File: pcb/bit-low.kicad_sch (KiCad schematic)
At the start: 6 parts, among them Q893 2N7002b, Q894 2N7002b, Q895 2N7002b

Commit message: Faster.
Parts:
- Q886: renamed from Q893; value 2N7002b -> 2N7002K; LCSC C8545 -> C181083
- Q887: renamed from Q894; value 2N7002b -> 2N7002K; LCSC C8545 -> C181083
- Q888: renamed from Q895; value 2N7002b -> 2N7002K; LCSC C8545 -> C181083
- renumbered R399 to R396, R400 to R397
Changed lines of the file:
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@@
   (symbol (lib_id "power:VCC") (at 184.15 44.45 0)
     (in_bom yes) (on_board yes)
-    (property "Reference" "#PWR0826" (id 0) (at 184.15 48.26 0)
+    (property "Reference" "#PWR0818" (id 0) (at 184.15 48.26 0)
       (effects (font (size 1.27 1.27)) hide)
     )
@@
   (symbol (lib_id "power:VCC") (at 200.66 40.64 0)
     (in_bom yes) (on_board yes)
-    (property "Reference" "#PWR0825" (id 0) (at 200.66 44.45 0)
+    (property "Reference" "#PWR0817" (id 0) (at 200.66 44.45 0)
       (effects (font (size 1.27 1.27)) hide)
     )
@@
   (symbol (lib_id "power:VCC") (at 220.98 71.12 0)
     (in_bom yes) (on_board yes)
-    (property "Reference" "#PWR0828" (id 0) (at 220.98 74.93 0)
+    (property "Reference" "#PWR0820" (id 0) (at 220.98 74.93 0)
       (effects (font (size 1.27 1.27)) hide)
     )
@@
   (symbol (lib_id "power:GND") (at 95.25 140.97 0)
     (in_bom yes) (on_board yes)
-    (property "Reference" "#PWR0830" (id 0) (at 95.25 147.32 0)
+    (property "Reference" "#PWR0822" (id 0) (at 95.25 147.32 0)
       (effects (font (size 1.27 1.27)) hide)
     )
@@
   (symbol (lib_id "power:GND") (at 184.15 52.07 0)
     (in_bom yes) (on_board yes)
-    (property "Reference" "#PWR0827" (id 0) (at 184.15 58.42 0)
+    (property "Reference" "#PWR0819" (id 0) (at 184.15 58.42 0)
       (effects (font (size 1.27 1.27)) hide)
     )
@@
   (symbol (lib_id "power:GND") (at 220.98 109.22 0)
     (in_bom yes) (on_board yes)
-    (property "Reference" "#PWR0829" (id 0) (at 220.98 115.57 0)
+    (property "Reference" "#PWR0821" (id 0) (at 220.98 115.57 0)
       (effects (font (size 1.27 1.27)) hide)
     )
@@
   (symbol (lib_id "Device:R") (at 200.66 44.45 0)
     (in_bom yes) (on_board yes)
-    (property "Reference" "R399" (id 0) (at 202.438 43.2816 0)
+    (property "Reference" "R396" (id 0) (at 202.438 43.2816 0)
       (effects (font (size 1.27 1.27)) (justify left))
     )
@@
   (symbol (lib_id "Device:R") (at 220.98 74.93 0)
     (in_bom yes) (on_board yes)
-    (property "Reference" "R400" (id 0) (at 222.758 73.7616 0)
+    (property "Reference" "R397" (id 0) (at 222.758 73.7616 0)
       (effects (font (size 1.27 1.27)) (justify left))
     )
@@
   (symbol (lib_id "Transistor_FET:2N7002") (at 92.71 135.89 0)
     (in_bom yes) (on_board yes)
-    (property "Reference" "Q895" (id 0) (at 97.9424 134.7216 0)
-      (effects (font (size 1.27 1.27)) (justify left))
-    )
-    (property "Value" "2N7002b" (id 1) (at 97.942 137.033 0)
+    (property "Reference" "Q888" (id 0) (at 97.9424 134.7216 0)
+      (effects (font (size 1.27 1.27)) (justify left))
+    )
+    (property "Value" "2N7002K" (id 1) (at 97.942 137.033 0)
       (effects (font (size 1.27 1.27)) (justify left))
     )
@@
       (effects (font (size 1.27 1.27) italic) (justify left) hide)
     )
-    (property "Datasheet" "https://www.fairchildsemi.com/datasheets/2N/2N7002.pdf" (id 3) (at 92.71 135.89 0)
+    (property "Datasheet" "https://datasheet.lcsc.com/szlcsc/Guangdong-Hottech-2N7002K_C181083.pdf" (id 3) (at 92.71 135.89 0)
       (effects (font (size 1.27 1.27)) (justify left) hide)
     )
-    (property "LCSC" "C8545" (id 4) (at 92.71 135.89 0)
+    (property "LCSC" "C181083" (id 4) (at 92.71 135.89 0)
       (effects (font (size 1.27 1.27)) hide)
     )
@@
   (symbol (lib_id "Transistor_FET:2N7002") (at 218.44 93.98 0)
     (in_bom yes) (on_board yes)
-    (property "Reference" "Q893" (id 0) (at 223.6724 92.8116 0)
-      (effects (font (size 1.27 1.27)) (justify left))
-    )
-    (property "Value" "2N7002b" (id 1) (at 223.672 95.123 0)
+    (property "Reference" "Q886" (id 0) (at 223.6724 92.8116 0)
+      (effects (font (size 1.27 1.27)) (justify left))
+    )
+    (property "Value" "2N7002K" (id 1) (at 223.672 95.123 0)
       (effects (font (size 1.27 1.27)) (justify left))
     )
@@
       (effects (font (size 1.27 1.27) italic) (justify left) hide)
     )
-    (property "Datasheet" "https://www.fairchildsemi.com/datasheets/2N/2N7002.pdf" (id 3) (at 218.44 93.98 0)
+    (property "Datasheet" "https://datasheet.lcsc.com/szlcsc/Guangdong-Hottech-2N7002K_C181083.pdf" (id 3) (at 218.44 93.98 0)
       (effects (font (size 1.27 1.27)) (justify left) hide)
     )
-    (property "LCSC" "C8545" (id 4) (at 218.44 93.98 0)
+    (property "LCSC" "C181083" (id 4) (at 218.44 93.98 0)
       (effects (font (size 1.27 1.27)) hide)
     )
@@
   (symbol (lib_id "Transistor_FET:2N7002") (at 218.44 104.14 0)
     (in_bom yes) (on_board yes)
-    (property "Reference" "Q894" (id 0) (at 223.6724 102.9716 0)
-      (effects (font (size 1.27 1.27)) (justify left))
-    )
-    (property "Value" "2N7002b" (id 1) (at 223.672 105.283 0)
+    (property "Reference" "Q887" (id 0) (at 223.6724 102.9716 0)
+      (effects (font (size 1.27 1.27)) (justify left))
+    )
+    (property "Value" "2N7002K" (id 1) (at 223.672 105.283 0)
       (effects (font (size 1.27 1.27)) (justify left))
     )
@@
       (effects (font (size 1.27 1.27) italic) (justify left) hide)
     )
-    (property "Datasheet" "https://www.fairchildsemi.com/datasheets/2N/2N7002.pdf" (id 3) (at 218.44 104.14 0)
+    (property "Datasheet" "https://datasheet.lcsc.com/szlcsc/Guangdong-Hottech-2N7002K_C181083.pdf" (id 3) (at 218.44 104.14 0)
       (effects (font (size 1.27 1.27)) (justify left) hide)
     )
-    (property "LCSC" "C8545" (id 4) (at 218.44 104.14 0)
-      (effects (font (size 1.27 1.27)) hide)
-    )
+    (property "LCSC" "C181083" (id 4) (at 218.44 104.14 0)
+      (effects (font (size 1.27 1.27)) hide)
+    )

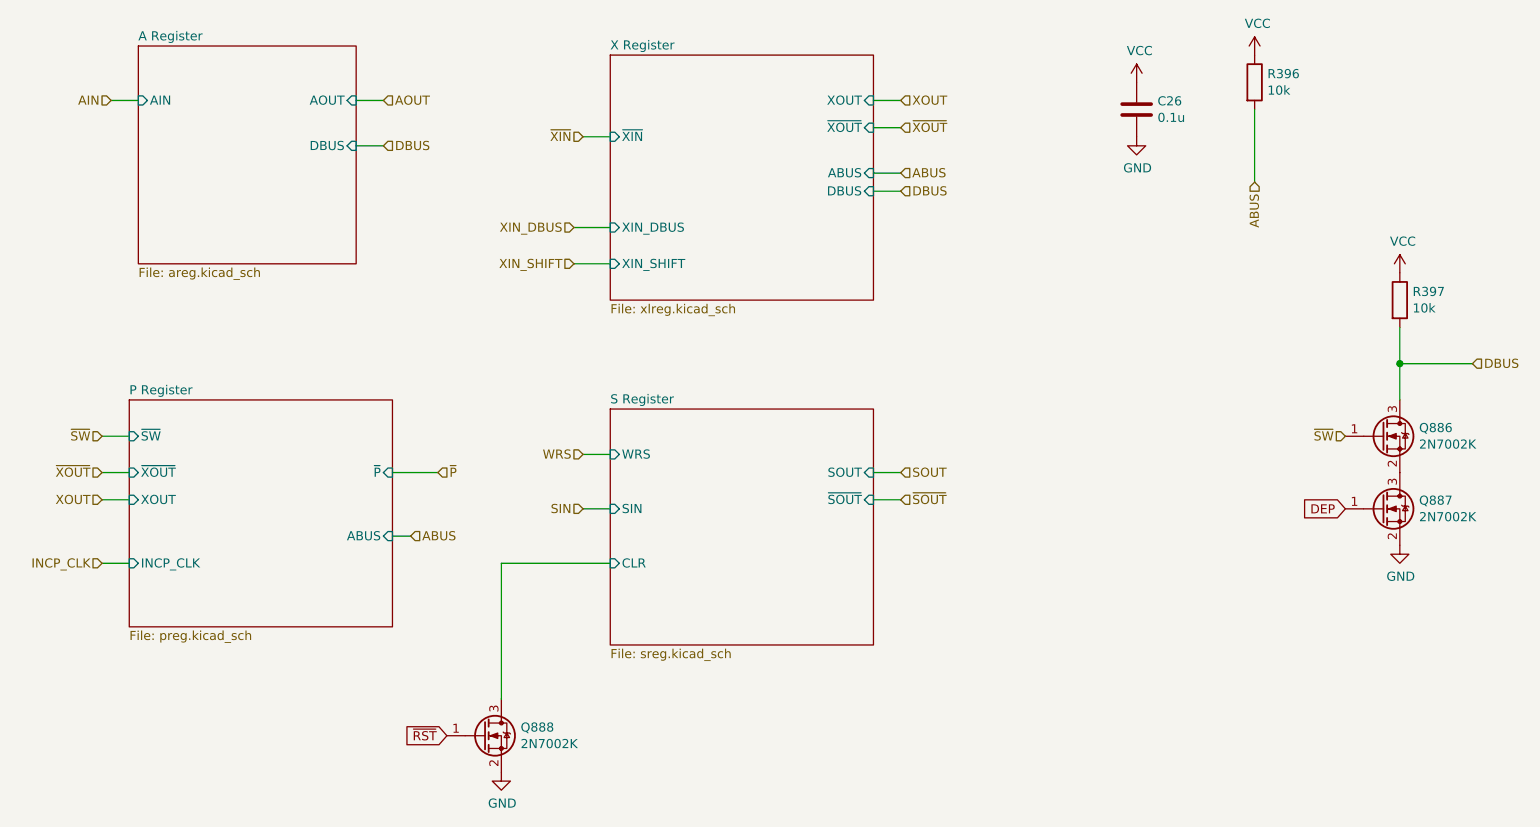
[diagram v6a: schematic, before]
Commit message: Fix flag for lea.
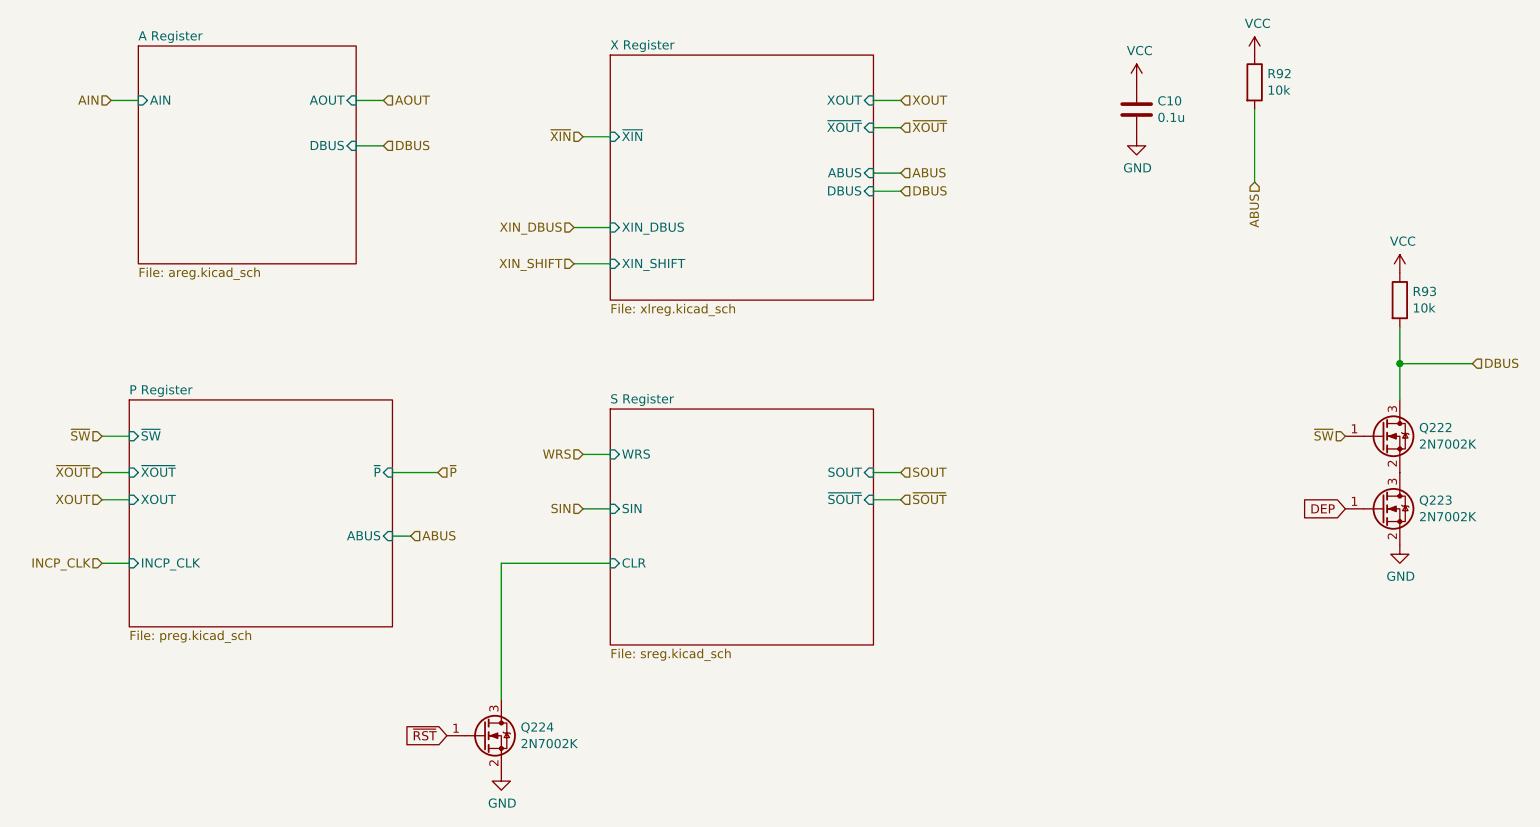
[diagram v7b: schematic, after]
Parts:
- renumbered C26 to C10, Q886 to Q222, Q887 to Q223, Q888 to Q224, R396 to R92, R397 to R93
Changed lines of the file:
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@@
   (symbol (lib_id "Device:R") (at 200.66 44.45 0)
     (in_bom yes) (on_board yes)
-    (property "Reference" "R396" (id 0) (at 202.438 43.2816 0)
+    (property "Reference" "R92" (id 0) (at 202.438 43.2816 0)
       (effects (font (size 1.27 1.27)) (justify left))
     )
@@
   (symbol (lib_id "Device:R") (at 220.98 74.93 0)
     (in_bom yes) (on_board yes)
-    (property "Reference" "R397" (id 0) (at 222.758 73.7616 0)
+    (property "Reference" "R93" (id 0) (at 222.758 73.7616 0)
       (effects (font (size 1.27 1.27)) (justify left))
     )
@@
   (symbol (lib_id "Device:C") (at 184.15 48.26 0)
     (in_bom yes) (on_board yes)
-    (property "Reference" "C26" (id 0) (at 187.071 47.0916 0)
+    (property "Reference" "C10" (id 0) (at 187.071 47.0916 0)
       (effects (font (size 1.27 1.27)) (justify left))
     )
@@
   (symbol (lib_id "Transistor_FET:2N7002") (at 92.71 135.89 0)
     (in_bom yes) (on_board yes)
-    (property "Reference" "Q888" (id 0) (at 97.9424 134.7216 0)
+    (property "Reference" "Q224" (id 0) (at 97.9424 134.7216 0)
       (effects (font (size 1.27 1.27)) (justify left))
     )
@@
   (symbol (lib_id "Transistor_FET:2N7002") (at 218.44 93.98 0)
     (in_bom yes) (on_board yes)
-    (property "Reference" "Q886" (id 0) (at 223.6724 92.8116 0)
+    (property "Reference" "Q222" (id 0) (at 223.6724 92.8116 0)
       (effects (font (size 1.27 1.27)) (justify left))
     )
@@
   (symbol (lib_id "Transistor_FET:2N7002") (at 218.44 104.14 0)
     (in_bom yes) (on_board yes)
-    (property "Reference" "Q887" (id 0) (at 223.6724 102.9716 0)
+    (property "Reference" "Q223" (id 0) (at 223.6724 102.9716 0)
       (effects (font (size 1.27 1.27)) (justify left))
     )

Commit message: Revision 3.
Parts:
- renumbered C10 to C26, Q222 to Q886, Q223 to Q887, Q224 to Q888, R92 to R396, R93 to R397
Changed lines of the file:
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@@
   (symbol (lib_id "Device:R") (at 200.66 44.45 0)
     (in_bom yes) (on_board yes)
-    (property "Reference" "R92" (id 0) (at 202.438 43.2816 0)
+    (property "Reference" "R396" (id 0) (at 202.438 43.2816 0)
       (effects (font (size 1.27 1.27)) (justify left))
     )
@@
   (symbol (lib_id "Device:R") (at 220.98 74.93 0)
     (in_bom yes) (on_board yes)
-    (property "Reference" "R93" (id 0) (at 222.758 73.7616 0)
+    (property "Reference" "R397" (id 0) (at 222.758 73.7616 0)
       (effects (font (size 1.27 1.27)) (justify left))
     )
@@
   (symbol (lib_id "Device:C") (at 184.15 48.26 0)
     (in_bom yes) (on_board yes)
-    (property "Reference" "C10" (id 0) (at 187.071 47.0916 0)
+    (property "Reference" "C26" (id 0) (at 187.071 47.0916 0)
       (effects (font (size 1.27 1.27)) (justify left))
     )
@@
   (symbol (lib_id "Transistor_FET:2N7002") (at 92.71 135.89 0)
     (in_bom yes) (on_board yes)
-    (property "Reference" "Q224" (id 0) (at 97.9424 134.7216 0)
+    (property "Reference" "Q888" (id 0) (at 97.9424 134.7216 0)
       (effects (font (size 1.27 1.27)) (justify left))
     )
@@
   (symbol (lib_id "Transistor_FET:2N7002") (at 218.44 93.98 0)
     (in_bom yes) (on_board yes)
-    (property "Reference" "Q222" (id 0) (at 223.6724 92.8116 0)
+    (property "Reference" "Q886" (id 0) (at 223.6724 92.8116 0)
       (effects (font (size 1.27 1.27)) (justify left))
     )
@@
   (symbol (lib_id "Transistor_FET:2N7002") (at 218.44 104.14 0)
     (in_bom yes) (on_board yes)
-    (property "Reference" "Q223" (id 0) (at 223.6724 102.9716 0)
+    (property "Reference" "Q887" (id 0) (at 223.6724 102.9716 0)
       (effects (font (size 1.27 1.27)) (justify left))
     )
